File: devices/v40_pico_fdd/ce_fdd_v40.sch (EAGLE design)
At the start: 65 parts, among them IC8 TLV1117LV33DCYR, J1 USB4125-GF-A, J3 ZL231-34PG, U1 RASPBERRY_PICOSMD-TH, U11 74LVC245, U12 74LVC245, U2 74LVC245, X10 FK 03 PWN, DC connector for P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

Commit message: updates to beeper - now on main fdd board, updates to panel connectors
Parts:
- removed C3: 100 nF, rcl:C-EUC0603
- removed T1: (no value), transistor:BC857A-PNP-SOT23-BEC
- added Q1: BC817-25LT3G, BC817-25LT3G:BC817-25LT3G
- added R37: 1k, rcl:R-EU_R0603
- added S1: DTSM-62N-V-B, DTSM-62N-V-B:DTSM-62N-V-B
- R20, R21: value 2k2 -> 10k
- R5: value 220R -> 0R
- SV2: device con-lstb:MA05-1 -> con-lstb:MA04-1
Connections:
- removed net ANALOG_BTNS: C3.1, R32.1, SV2.1, U1.GP27
- removed net RX0: U1.GP1
- removed net SCL: R21.1, SV2.3, U1.GP17
- removed net SDA: R20.1, SV2.2, U1.GP16
- new net BEEPER: R30.1, R31.1, U1.GP27
- new net CAPTIVE_BTN: R20.2, S1.COM_1, S1.COM_2, U1.GP1
- new net N$10: R37.2, SV2.2
- new net PANEL_RX: R32.2, U1.GP17
- new net PANEL_TX: R37.1, U1.GP16
- net 5V: now also R5.1, SV2.3
- net GND: now also JP2.2, Q1.E, R31.2, S1.NO_1, S1.NO_2, SV2.4; no longer C3.2, R5.2, SV2.5
- net N$3: now also Q1.B; no longer T1.B
- net N$4: now also LS1.-, Q1.C; no longer JP2.2, R30.1, R31.1
- net N$7: now also R5.2; no longer T1.C
- net N$9: now also R21.1, R32.1, SV2.1; no longer LS1.-, R5.1
- net STEP: no longer JP2.1
- net TX0: now also JP2.1
- net VCC: now also R20.1; no longer R20.2, R31.2, R32.2, SV2.4, T1.E
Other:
- note removed: "OLED i2c 0.91" connection"
- moved on the sheet: JP2, LS1

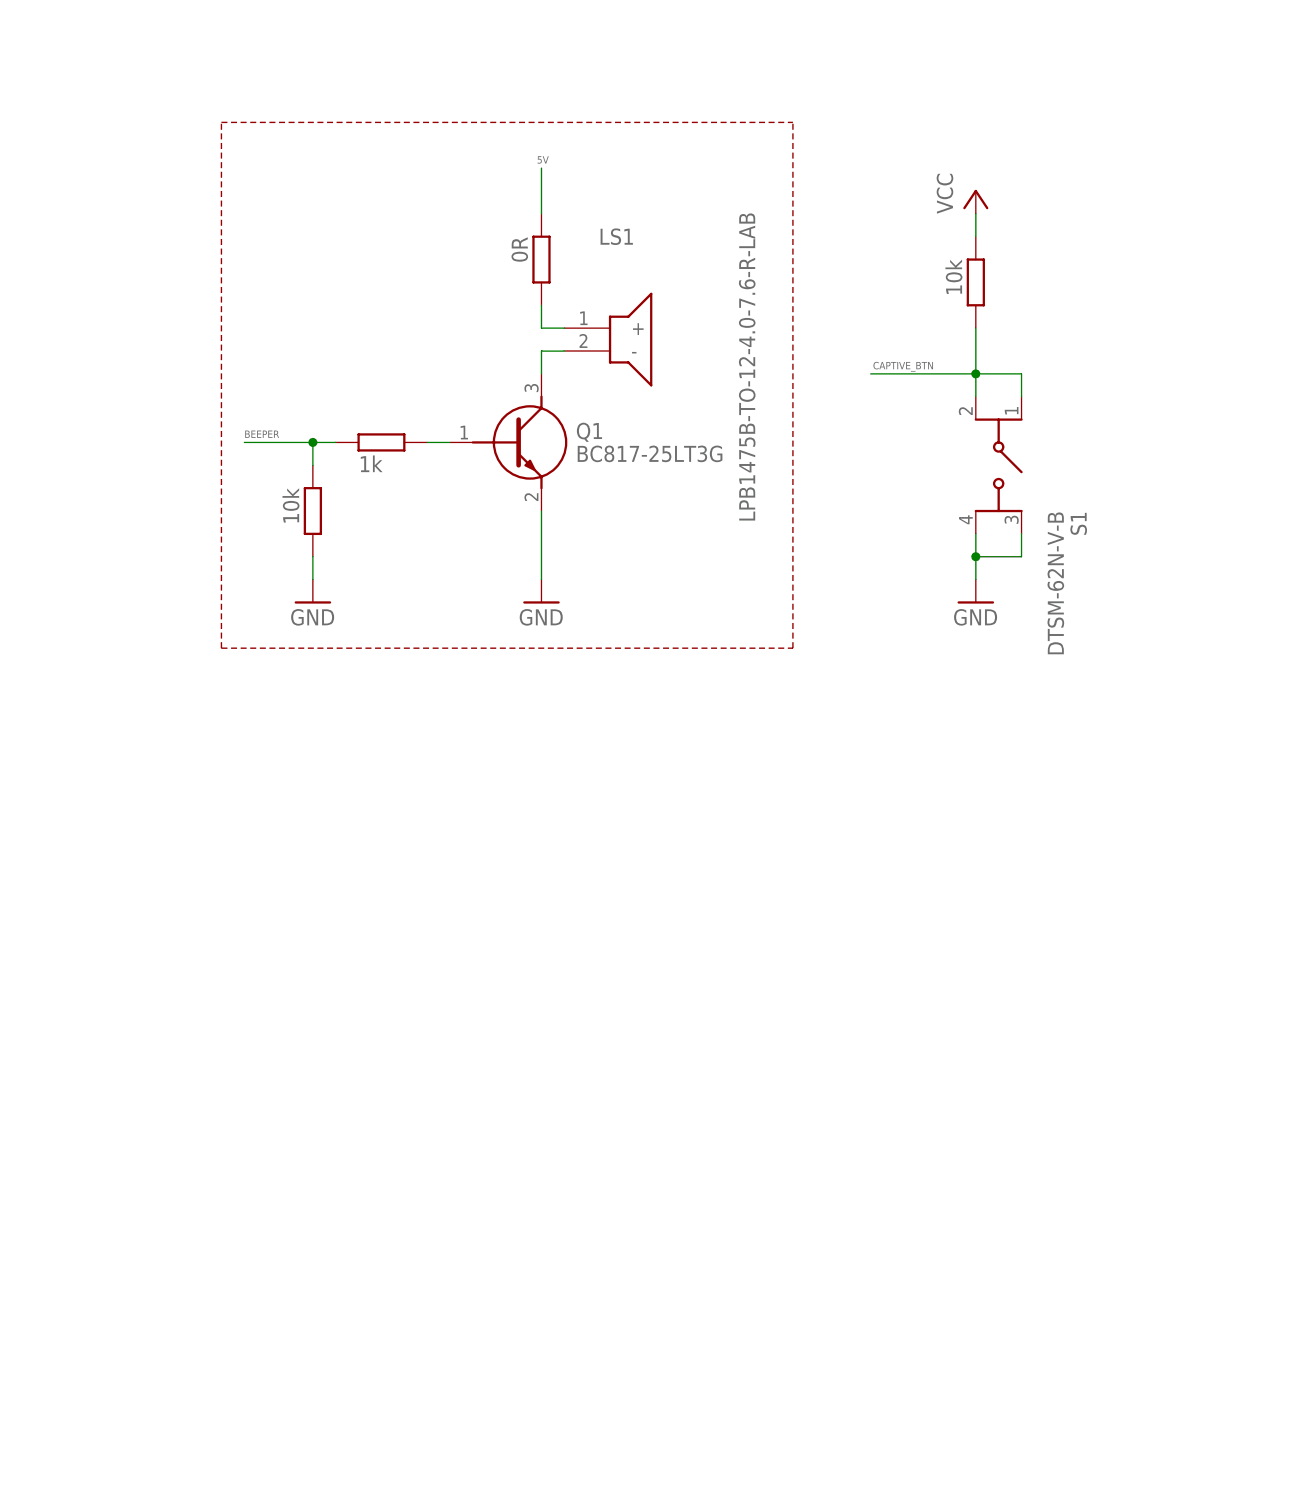
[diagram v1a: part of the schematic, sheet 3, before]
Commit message: changed button, added neopixel to fdd
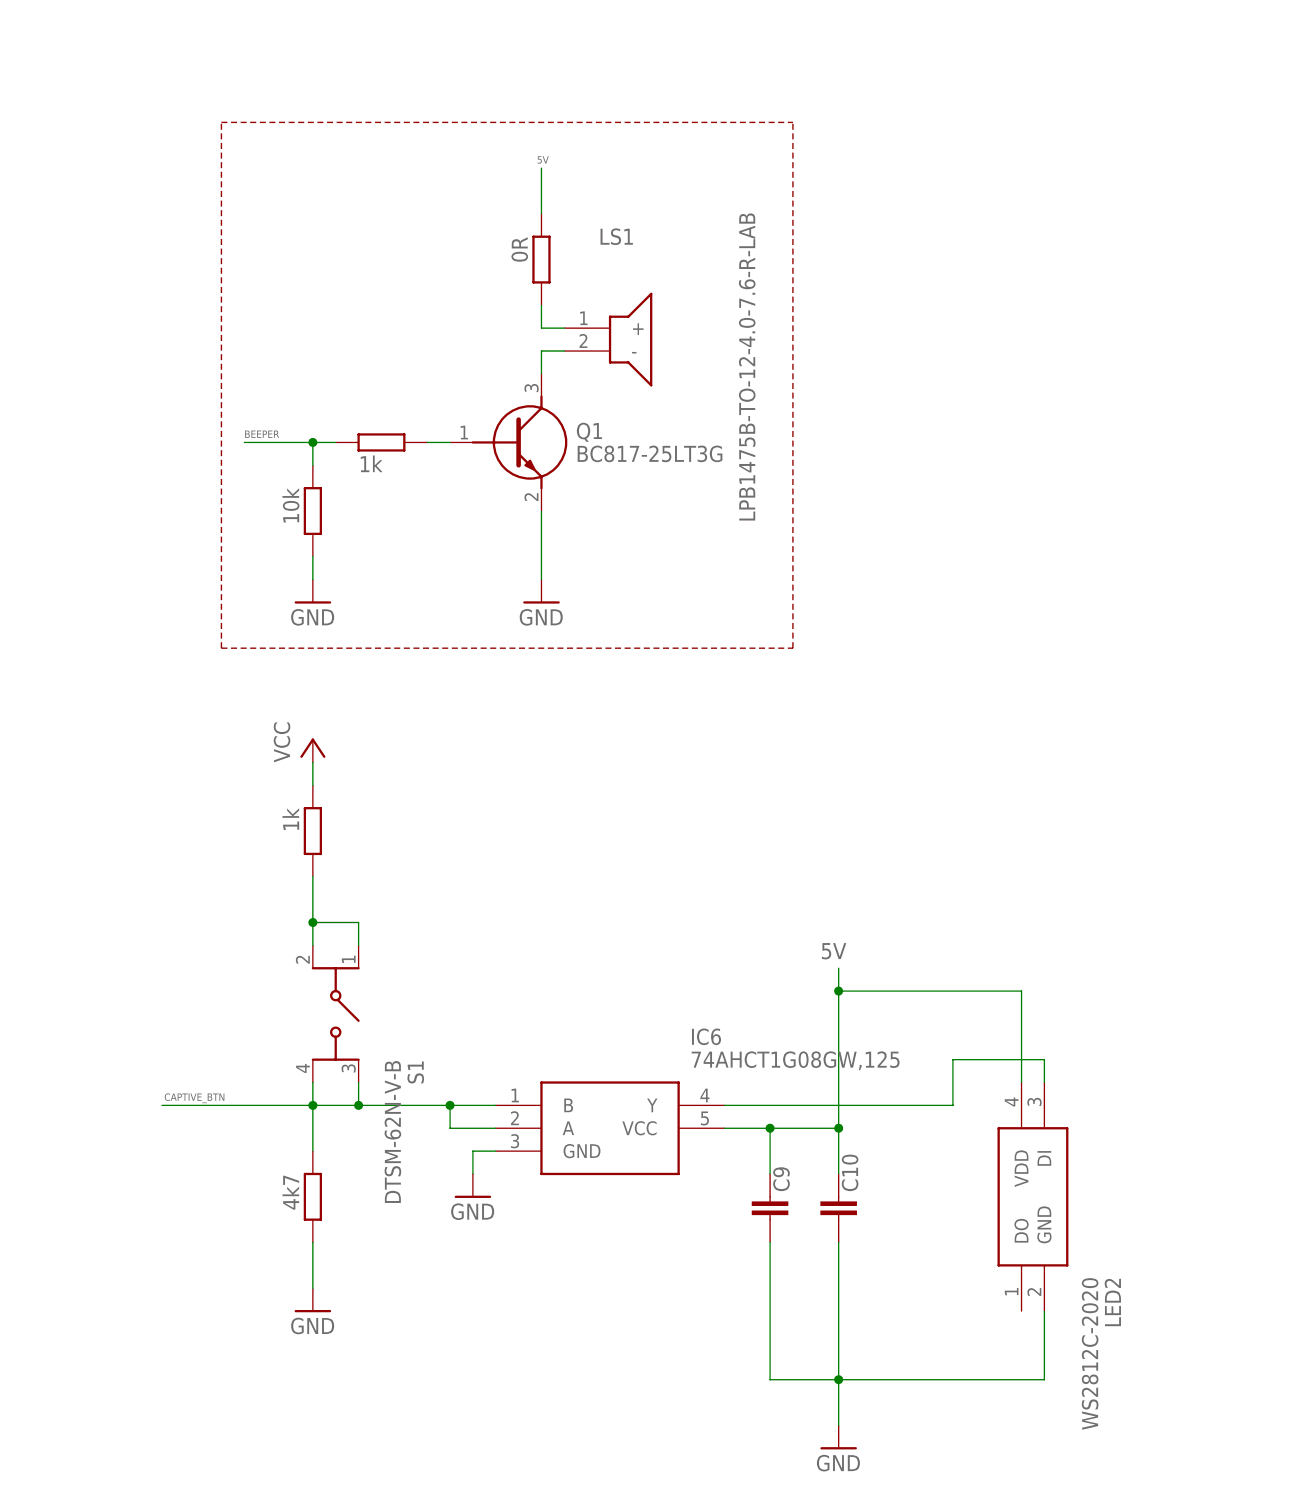
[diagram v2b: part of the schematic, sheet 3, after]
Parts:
- added C10, C9: 100 nF, rcl:C-EUC0603
- added IC6: 74AHCT1G08GW,125, 74AHCT1G08GW_125:74AHCT1G08GW,125
- added LED2: WS2812C-2020, WS2812C-2020:WS2812C-2020
- added R38: 4k7, rcl:R-EU_R0603
- R20: value 10k -> 1k
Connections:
- new net N$13: R20.2, S1.COM_1, S1.COM_2
- new net N$15: IC6.Y, LED2.DI
- net 5V: now also C10.1, C9.1, IC6.VCC, LED2.VDD
- net CAPTIVE_BTN: now also IC6.A, IC6.B, R38.1, S1.NO_1, S1.NO_2; no longer R20.2, S1.COM_1, S1.COM_2
- net GND: now also C10.2, C9.2, IC6.GND, LED2.GND, R38.2; no longer S1.NO_1, S1.NO_2
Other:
- moved on the sheet: S1
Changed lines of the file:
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@@
 <part name="S1" library="DTSM-62N-V-B" deviceset="DTSM-62N-V-B" device=""/>
 <part name="GND9" library="supply1" deviceset="GND" device=""/>
-<part name="R20" library="rcl" deviceset="R-EU_" device="R0603" value="10k"/>
+<part name="R20" library="rcl" deviceset="R-EU_" device="R0603" value="1k"/>
 <part name="P+12" library="supply1" deviceset="VCC" device=""/>
 <part name="SV2" library="con-lstb" deviceset="MA04-1" device=""/>
@@
 <part name="R37" library="rcl" deviceset="R-EU_" device="R0603" value="1k"/>
 <part name="P+1" library="supply1" deviceset="VCC" device=""/>
+<part name="R38" library="rcl" deviceset="R-EU_" device="R0603" value="4k7"/>
+<part name="C10" library="rcl" deviceset="C-EU" device="C0603" value="100 nF"/>
+<part name="GND12" library="supply1" deviceset="GND" device=""/>
+<part name="LED2" library="WS2812C-2020" deviceset="WS2812C-2020" device=""/>
+<part name="GND15" library="supply1" deviceset="GND" device=""/>
+<part name="C9" library="rcl" deviceset="C-EU" device="C0603" value="100 nF"/>
+<part name="IC6" library="74AHCT1G08GW_125" deviceset="74AHCT1G08GW,125" device=""/>
 </parts>
 <sheets>
@@
 <instance part="GND7" gate="1" x="-12.7" y="48.26"/>
 <instance part="Q1" gate="G$1" x="2.54" y="66.04"/>
-<instance part="S1" gate="G$1" x="66.04" y="71.12" rot="R270"/>
-<instance part="GND9" gate="1" x="60.96" y="48.26"/>
-<instance part="R20" gate="G$1" x="60.96" y="83.82" smashed="yes" rot="R270">
-<attribute name="VALUE" x="57.658" y="86.36" size="1.778" layer="96" rot="R270"/>
-</instance>
-<instance part="P+12" gate="VCC" x="60.96" y="93.98"/>
+<instance part="S1" gate="G$1" x="-7.62" y="10.16" rot="R270"/>
+<instance part="GND9" gate="1" x="-12.7" y="-30.48"/>
+<instance part="R20" gate="G$1" x="-12.7" y="22.86" smashed="yes" rot="R270">
+<attribute name="VALUE" x="-16.002" y="25.4" size="1.778" layer="96" rot="R270"/>
+</instance>
+<instance part="P+12" gate="VCC" x="-12.7" y="33.02"/>
 <instance part="SV2" gate="1" x="22.86" y="134.62" rot="R180"/>
 <instance part="JP2" gate="A" x="-152.4" y="162.56" rot="MR270"/>
@@
 </instance>
 <instance part="P+1" gate="VCC" x="10.16" y="157.48"/>
+<instance part="R38" gate="G$1" x="-12.7" y="-17.78" smashed="yes" rot="R270">
+<attribute name="VALUE" x="-16.002" y="-15.24" size="1.778" layer="96" rot="R270"/>
+</instance>
+<instance part="C10" gate="G$1" x="45.72" y="-17.78" smashed="yes">
+<attribute name="NAME" x="47.879" y="-17.272" size="1.778" layer="95" rot="R90"/>
+</instance>
+<instance part="GND12" gate="1" x="45.72" y="-45.72"/>
+<instance part="LED2" gate="G$1" x="68.58" y="-5.08" rot="R270"/>
+<instance part="GND15" gate="1" x="5.08" y="-17.78"/>
+<instance part="C9" gate="G$1" x="38.1" y="-17.78" smashed="yes">
+<attribute name="NAME" x="40.259" y="-17.272" size="1.778" layer="95" rot="R90"/>
+</instance>
+<instance part="IC6" gate="G$1" x="7.62" y="-7.62"/>
 </instances>
 <busses>
@@
 </segment>
 <segment>
-<pinref part="R20" gate="G$1" pin="1"/>
-<pinref part="P+12" gate="VCC" pin="VCC"/>
-<wire x1="60.96" y1="88.9" x2="60.96" y2="91.44" width="0.1524" layer="91"/>
-</segment>
-<segment>
 <pinref part="R21" gate="G$1" pin="2"/>
 <pinref part="P+1" gate="VCC" pin="VCC"/>
 <wire x1="10.16" y1="152.4" x2="10.16" y2="154.94" width="0.1524" layer="91"/>
+</segment>
+<segment>
+<pinref part="R20" gate="G$1" pin="1"/>
+<pinref part="P+12" gate="VCC" pin="VCC"/>
+<wire x1="-12.7" y1="27.94" x2="-12.7" y2="30.48" width="0.1524" layer="91"/>
 </segment>
 </net>
@@
 </segment>
 <segment>
-<pinref part="S1" gate="G$1" pin="NO_2"/>
-<pinref part="GND9" gate="1" pin="GND"/>
-<wire x1="60.96" y1="55.88" x2="60.96" y2="53.34" width="0.1524" layer="91"/>
-<pinref part="S1" gate="G$1" pin="NO_1"/>
-<wire x1="60.96" y1="53.34" x2="60.96" y2="50.8" width="0.1524" layer="91"/>
-<wire x1="66.04" y1="55.88" x2="66.04" y2="53.34" width="0.1524" layer="91"/>
-<wire x1="66.04" y1="53.34" x2="60.96" y2="53.34" width="0.1524" layer="91"/>
-<junction x="60.96" y="53.34"/>
-</segment>
-<segment>
 <pinref part="JP2" gate="A" pin="2"/>
 <pinref part="GND11" gate="1" pin="GND"/>
 <wire x1="-149.86" y1="160.02" x2="-147.32" y2="160.02" width="0.1524" layer="91"/>
 <wire x1="-147.32" y1="160.02" x2="-147.32" y2="157.48" width="0.1524" layer="91"/>
+</segment>
+<segment>
+<pinref part="GND9" gate="1" pin="GND"/>
+<pinref part="R38" gate="G$1" pin="2"/>
+<wire x1="-12.7" y1="-27.94" x2="-12.7" y2="-22.86" width="0.1524" layer="91"/>
+</segment>
+<segment>
+<pinref part="GND12" gate="1" pin="GND"/>
+<pinref part="C10" gate="G$1" pin="2"/>
+<wire x1="45.72" y1="-43.18" x2="45.72" y2="-38.1" width="0.1524" layer="91"/>
+<pinref part="LED2" gate="G$1" pin="GND"/>
+<wire x1="45.72" y1="-38.1" x2="45.72" y2="-22.86" width="0.1524" layer="91"/>
+<wire x1="68.58" y1="-30.48" x2="68.58" y2="-38.1" width="0.1524" layer="91"/>
+<wire x1="68.58" y1="-38.1" x2="45.72" y2="-38.1" width="0.1524" layer="91"/>
+<junction x="45.72" y="-38.1"/>
+<pinref part="C9" gate="G$1" pin="2"/>
+<wire x1="38.1" y1="-22.86" x2="38.1" y2="-38.1" width="0.1524" layer="91"/>
+<wire x1="38.1" y1="-38.1" x2="45.72" y2="-38.1" width="0.1524" layer="91"/>
+</segment>
+<segment>
+<wire x1="5.08" y1="-12.7" x2="5.08" y2="-15.24" width="0.1524" layer="91"/>
+<wire x1="7.62" y1="-12.7" x2="5.08" y2="-12.7" width="0.1524" layer="91"/>
+<pinref part="GND15" gate="1" pin="GND"/>
+<pinref part="IC6" gate="G$1" pin="GND"/>
 </segment>
 </net>
@@
 <pinref part="SV2" gate="1" pin="3"/>
 </segment>
+<segment>
+<pinref part="C10" gate="G$1" pin="1"/>
+<wire x1="45.72" y1="-15.24" x2="45.72" y2="-10.16" width="0.1524" layer="91"/>
+<label x="43.688" y="8.636" size="1.778" layer="95"/>
+<pinref part="LED2" gate="G$1" pin="VDD"/>
+<wire x1="45.72" y1="-10.16" x2="45.72" y2="5.08" width="0.1524" layer="91"/>
+<wire x1="45.72" y1="5.08" x2="45.72" y2="7.62" width="0.1524" layer="91"/>
+<wire x1="66.04" y1="-5.08" x2="66.04" y2="5.08" width="0.1524" layer="91"/>
+<wire x1="66.04" y1="5.08" x2="45.72" y2="5.08" width="0.1524" layer="91"/>
+<junction x="45.72" y="5.08"/>
+<wire x1="33.02" y1="-10.16" x2="38.1" y2="-10.16" width="0.1524" layer="91"/>
+<junction x="45.72" y="-10.16"/>
+<pinref part="C9" gate="G$1" pin="1"/>
+<wire x1="38.1" y1="-10.16" x2="45.72" y2="-10.16" width="0.1524" layer="91"/>
+<wire x1="38.1" y1="-15.24" x2="38.1" y2="-10.16" width="0.1524" layer="91"/>
+<junction x="38.1" y="-10.16"/>
+<pinref part="IC6" gate="G$1" pin="VCC"/>
+</segment>
 </net>
 <net name="PANEL_RX" class="0">
@@
 <net name="CAPTIVE_BTN" class="0">
 <segment>
-<pinref part="S1" gate="G$1" pin="COM_2"/>
-<pinref part="S1" gate="G$1" pin="COM_1"/>
-<wire x1="66.04" y1="71.12" x2="66.04" y2="73.66" width="0.1524" layer="91"/>
-<pinref part="R20" gate="G$1" pin="2"/>
-<wire x1="60.96" y1="78.74" x2="60.96" y2="73.66" width="0.1524" layer="91"/>
-<wire x1="60.96" y1="73.66" x2="60.96" y2="71.12" width="0.1524" layer="91"/>
-<wire x1="60.96" y1="73.66" x2="66.04" y2="73.66" width="0.1524" layer="91"/>
-<junction x="60.96" y="73.66"/>
-<wire x1="60.96" y1="73.66" x2="49.276" y2="73.66" width="0.1524" layer="91"/>
-<label x="49.53" y="74.168" size="0.8128" layer="95" font="vector" ratio="20"/>
+<wire x1="-12.7" y1="-7.62" x2="-29.464" y2="-7.62" width="0.1524" layer="91"/>
+<label x="-29.21" y="-7.112" size="0.8128" layer="95" font="vector" ratio="20"/>
+<pinref part="S1" gate="G$1" pin="NO_2"/>
+<pinref part="R38" gate="G$1" pin="1"/>
+<wire x1="-12.7" y1="-5.08" x2="-12.7" y2="-7.62" width="0.1524" layer="91"/>
+<pinref part="S1" gate="G$1" pin="NO_1"/>
+<wire x1="-12.7" y1="-7.62" x2="-12.7" y2="-12.7" width="0.1524" layer="91"/>
+<wire x1="-7.62" y1="-5.08" x2="-7.62" y2="-7.62" width="0.1524" layer="91"/>
+<wire x1="-7.62" y1="-7.62" x2="-12.7" y2="-7.62" width="0.1524" layer="91"/>
+<junction x="-12.7" y="-7.62"/>
+<pinref part="IC6" gate="G$1" pin="B"/>
+<wire x1="-7.62" y1="-7.62" x2="2.54" y2="-7.62" width="0.1524" layer="91"/>
+<junction x="-7.62" y="-7.62"/>
+<wire x1="2.54" y1="-7.62" x2="7.62" y2="-7.62" width="0.1524" layer="91"/>
+<wire x1="2.54" y1="-10.16" x2="7.62" y2="-10.16" width="0.1524" layer="91"/>
+<pinref part="IC6" gate="G$1" pin="A"/>
+<wire x1="2.54" y1="-10.16" x2="2.54" y2="-7.62" width="0.1524" layer="91"/>
+<junction x="2.54" y="-7.62"/>
 </segment>
 <segment>
@@
 </segment>
 </net>
+<net name="N$13" class="0">
+<segment>
+<pinref part="R20" gate="G$1" pin="2"/>
+<pinref part="S1" gate="G$1" pin="COM_2"/>
+<wire x1="-12.7" y1="17.78" x2="-12.7" y2="12.7" width="0.1524" layer="91"/>
+<pinref part="S1" gate="G$1" pin="COM_1"/>
+<wire x1="-12.7" y1="12.7" x2="-12.7" y2="10.16" width="0.1524" layer="91"/>
+<wire x1="-7.62" y1="10.16" x2="-7.62" y2="12.7" width="0.1524" layer="91"/>
+<wire x1="-7.62" y1="12.7" x2="-12.7" y2="12.7" width="0.1524" layer="91"/>
+<junction x="-12.7" y="12.7"/>
+</segment>
+</net>
+<net name="N$15" class="0">
+<segment>
+<pinref part="LED2" gate="G$1" pin="DI"/>
+<wire x1="33.02" y1="-7.62" x2="58.42" y2="-7.62" width="0.1524" layer="91"/>
+<wire x1="58.42" y1="-7.62" x2="58.42" y2="-2.54" width="0.1524" layer="91"/>
+<wire x1="58.42" y1="-2.54" x2="68.58" y2="-2.54" width="0.1524" layer="91"/>
+<wire x1="68.58" y1="-2.54" x2="68.58" y2="-5.08" width="0.1524" layer="91"/>
+<pinref part="IC6" gate="G$1" pin="Y"/>
+</segment>
+</net>
